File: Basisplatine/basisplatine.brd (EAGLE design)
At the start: 160 x 100 mm, 27 parts, among them IC1 RASPBERRY_PI_ZERO_W__V1.3_, IC2 MEGA8-AI

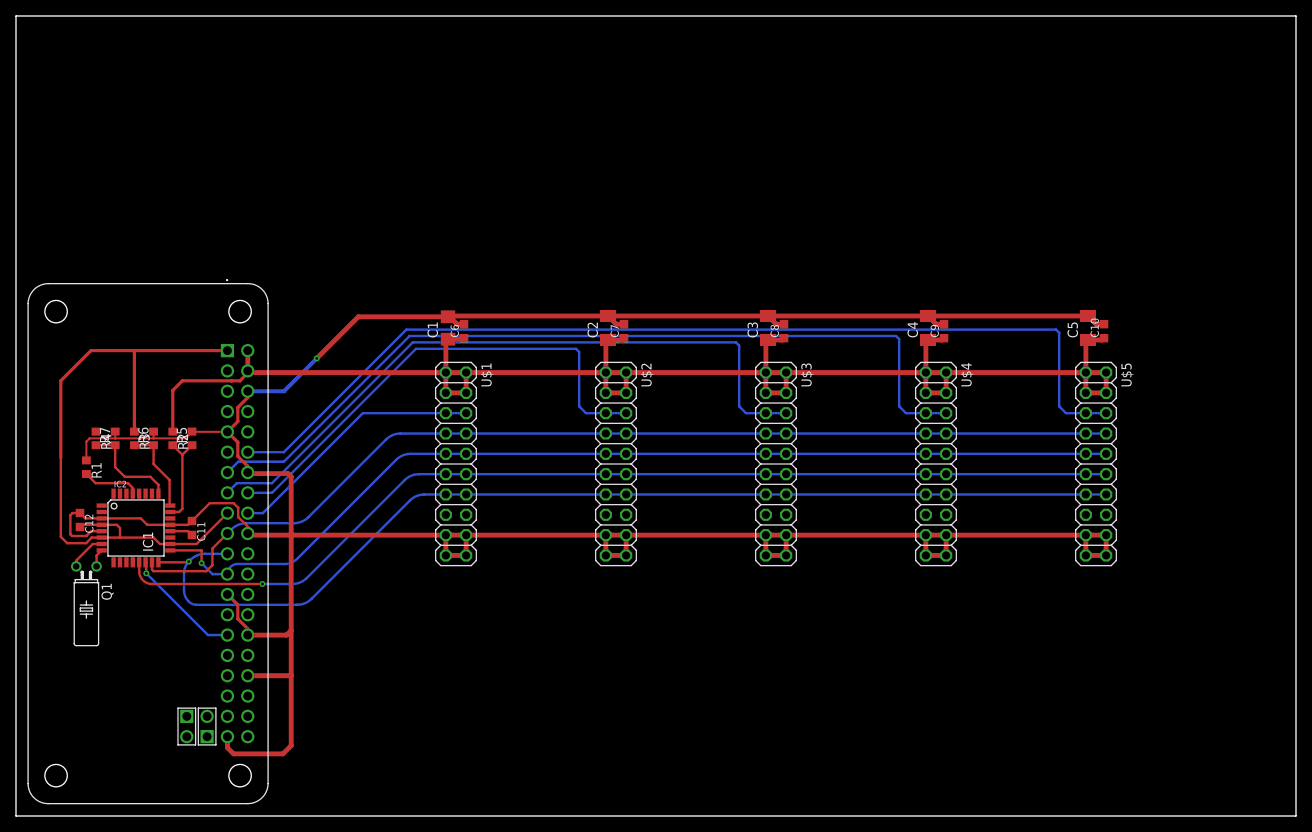
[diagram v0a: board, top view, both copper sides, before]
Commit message: added battery managment
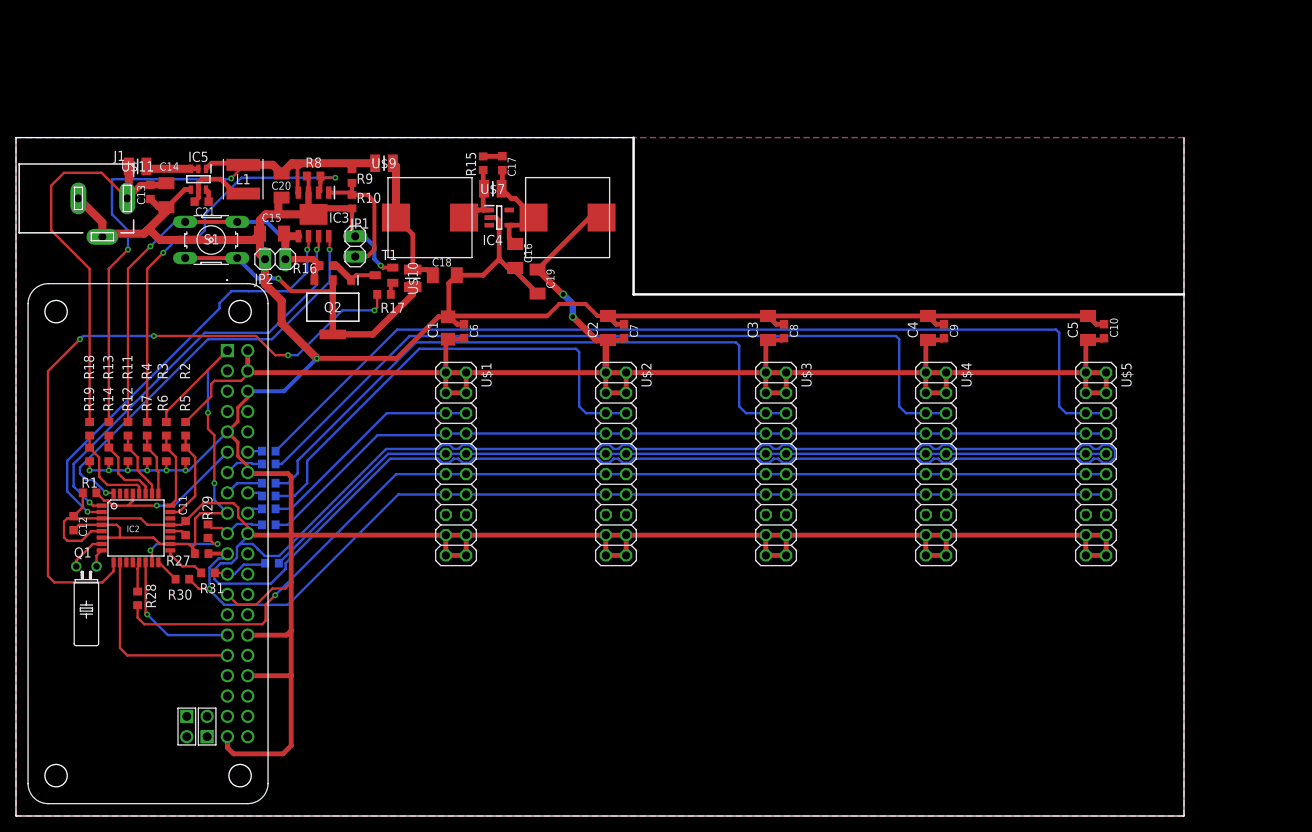
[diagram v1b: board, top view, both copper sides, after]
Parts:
- added C13: 100n, rcl:C0603K
- added C14, C15, C16, C19, C20: 10u, rcl:C1206K
- added C17, C21: 120p, rcl:C0603K
- added C18: 2u2, rcl:C1206K
- added IC3: DIO5158XS8, basisplatine_lib:SOIC127P600X170-9N
- added IC4: TPS613222ADBVR, basisplatine_lib:SOT95P280X145-5N
- added IC5: AP63205WU-7, basisplatine_lib:SOT95P280X100-6N
- added J1: DCJ0202, con-jack:DCJ0202
- added JP1, JP2: (no value), pinhead:1X02
- added L1: SRN5040TA-4R7M, basisplatine_lib:SRN5040TA4R7M
- added Q2: NTF5P03T3G, basisplatine_lib:SOT230P700X175-4N
- added R10, R11, R12, R13, R14, R18, R19, R9: (no value), rcl:R0603
- added R15: 5R, rcl:R0603
- added R16, R17, R29, R30, R31: 10k, rcl:R0603
- added R20, R21, R22, R23, R24, R25, R26, R28: 100R, rcl:R0603
- added R27: 2k, rcl:R0603
- added R8: 1218R, rcl:R0603
- added S1: (no value), switch-omron:B3F-10XX
- added T1: (no value), transistor:SOT23-BEC
- added U$10, U$11, U$7, U$9: SK1035-TP, basisplatine_lib:INDC2520X120N
- added U$6, U$8: SRP1038C-2R2M, basisplatine_lib:SRP1038C-2R2M
- moved R4 6.51 mm to (16.4, 48.4)
- moved R7 4.47 mm to (16.4, 45.2), turned to 270 degrees
- moved R3 4.18 mm to (18.8, 48.4)
- moved R1 3.22 mm to (9.20, 40.4), turned to 0 degrees
- moved R6 2.56 mm to (18.8, 45.2), turned to 270 degrees
- moved R5 2.15 mm to (21.2, 45.2), turned to 270 degrees
- moved R2 2.00 mm to (21.2, 48.4)
- moved C12 0.89 mm to (7.20, 36.6)
- moved C11 0.80 mm to (21.2, 36.0)
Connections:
- net N$7 renamed ADC0
- net N$8 renamed ADC1
- net N$9 renamed ADC2
- new net ADC3: IC2.26, R11.2, R12.1
- new net ADC4: IC2.27, R13.2, R14.1
- new net ADC5: IC2.28, R18.2, R19.1
- new net BOOST_EN: IC2.9, R17.2
- new net CHARGE_EN: IC2.32, IC3.8
- new net ISET: IC3.2, R4.1, R8.2
- new net N$1: IC4.1, R15.2, U$6.P$2, U$7.1
- new net N$10: Q2.1, R16.2, T1.C
- new net N$11: R17.1, T1.B
- new net N$12: Q2.2, Q2.4, S1.1, S1.2, U$10.1
- new net N$13: C21.2, IC5.6
- new net N$15: IC1.18, R22.1
- new net N$16: IC1.16, R23.1
- new net N$17: IC1.15, R24.1
- new net N$18: IC1.13, R25.1
- new net N$19: IC1.12, R26.1
- new net N$20: IC2.13, R28.1
- new net N$21: IC2.15, R29.1
- new net N$22: IC2.16, R30.1
- new net N$23: IC2.17, R31.1
- new net N$5: IC5.2, IC5.3, U$11.2
- new net N$7: C17.1, R15.1
- new net N$8: C16.1, C17.2, IC4.4, U$7.2, U$8.P$1
- new net N$9: C18.1, U$10.2, U$6.P$1, U$9.2
- new net SHUTDOWN: IC1.31, IC2.10
- new net SPI_CLK_R: IC1.23, R20.2, R31.2
- new net SPI_MOSI_R: IC1.19, R21.1, R29.2
- new net STATUS_CHARGE: IC2.1, IC3.7
- new net STATUS_DONE: IC2.2, IC3.6
- new net TEMP: IC3.1, JP1.2, R10.2, R9.1
- new net VIN: C20.1, IC3.4, IC5.1, L1.2, R13.1, R9.2, U$9.1
- new net VJACK: C13.2, C14.1, J1.1, R18.1, U$11.1
- net +3V3: now also R27.2
- net +5V: now also C19.1, U$8.P$2
- net CLOCK_EN: now also IC1.11
- net GND: now also C13.1, C14.2, C15.2, C16.2, C18.2, C19.2, C20.2, IC3.3, IC3.9, IC4.2, IC5.4, J1.2, J1.3, JP1.1, JP2.2, R10.1, R12.2, R14.2, R19.2, R8.1, T1.E
- net N$6: now also C21.1, IC5.5, L1.1; no longer IC1.11
- net SAMPLE: now also R28.2; no longer IC2.13
- net SPI_CLK: now also R20.1; no longer IC1.23, IC2.17
- net SPI_MISO: now also R27.1, R30.2; no longer IC2.16
- net SPI_MOSI: now also R21.2; no longer IC1.19, IC2.15
- net SS1: now also R22.2; no longer IC1.18
- net SS2: now also R23.2; no longer IC1.16
- net SS3: now also R24.2; no longer IC1.15
- net SS4: now also R25.2; no longer IC1.13
- net SS5: now also R26.2; no longer IC1.12
- net VBAT: now also C15.1, IC3.5, JP2.1, Q2.3, R11.1, R16.1, S1.3, S1.4; no longer R4.1
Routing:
- net GND: track 401.2 -> 780.9 mm, vias 1 -> 8
- net VIN: track 0.00 -> 93.0 mm, vias 0 -> 2
- net BOOST_EN: track 0.00 -> 83.9 mm, vias 0 -> 4
- net VBAT: track 0.00 -> 56.4 mm, vias 0 -> 1
- net STATUS_DONE: track 0.00 -> 53.9 mm, vias 0 -> 2
- net STATUS_CHARGE: track 0.00 -> 53.2 mm, vias 0 -> 2
- net ISET: track 0.00 -> 52.8 mm, vias 0 -> 2
- net VJACK: track 0.00 -> 52.8 mm
- net CHARGE_EN: track 0.00 -> 52.6 mm, vias 0 -> 2
- net N$12: track 0.00 -> 39.9 mm, vias 0 -> 1
- net SHUTDOWN: track 0.00 -> 24.5 mm
- net +5V: track 195.8 -> 215.3 mm, vias 0 -> 2
- net SPI_MOSI: track 128.1 -> 108.8 mm
- net +3V3: track 81.9 -> 62.7 mm, vias 0 -> 2
- net N$9: track 0.00 -> 17.1 mm
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- added copper zone on layer 1, net GND
- added copper zone on layer 16, net GND
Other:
- board size 160 x 100 mm -> 146 x 84.8 mm

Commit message: Added dampening Cs on SPI and RJ45
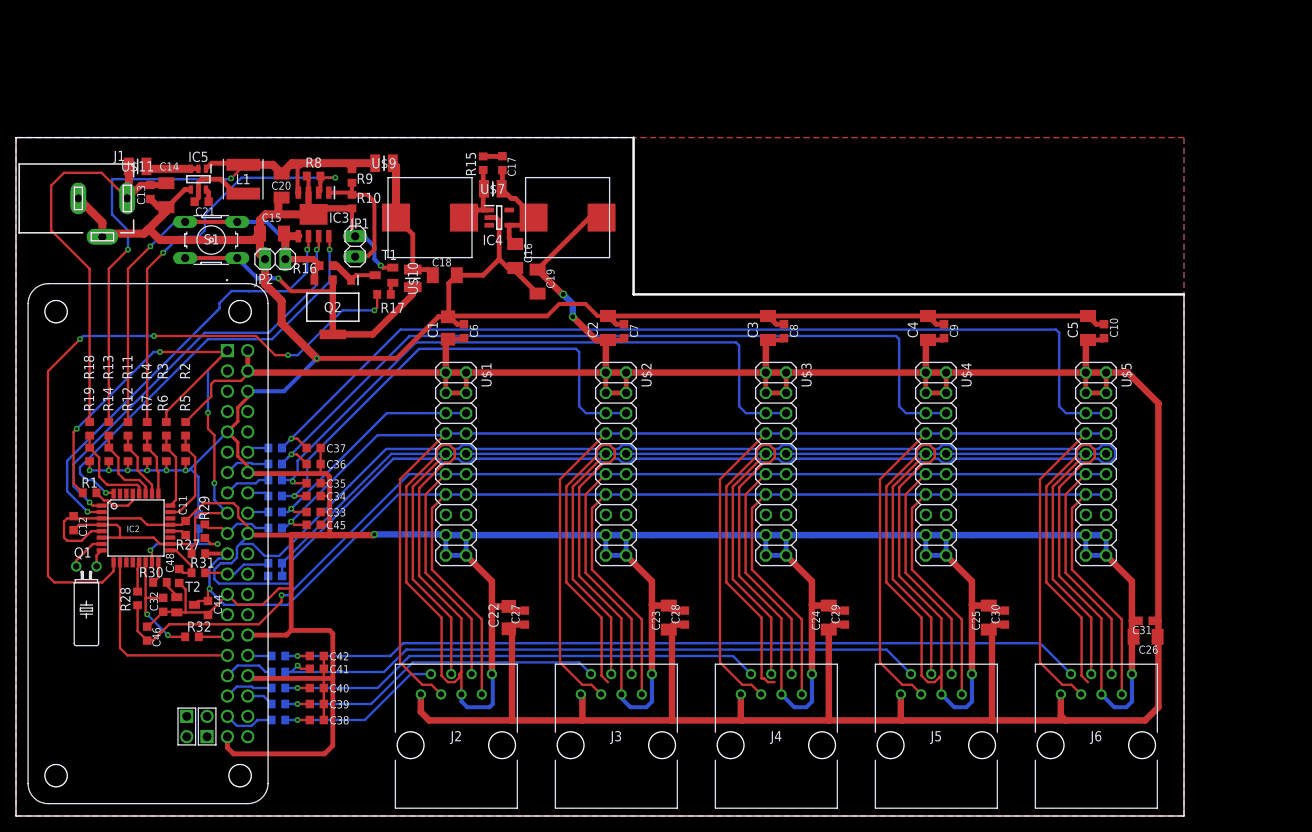
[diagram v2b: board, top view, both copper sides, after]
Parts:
- added C22: (no value), rcl:C1206
- added C23, C24, C25, C26: 2u2, rcl:C1206K
- added C27, C28, C29, C30, C31: 100n, rcl:C0603K
- added C32, C33, C34, C35, C36, C37, C38, C39, C40, C41, C42, C43, C44, C45, C46, C47, C48: (no value), rcl:C0603K
- added J2, J3, J4, J5, J6: 54601-908WPLF, basisplatine_lib:54601908WPLF
- added R32, R33, R34, R35, R36, R37: 100R, rcl:R0603
- added T2: (no value), transistor:SOT23-BEC
- moved R30 2.83 mm to (18.0, 29.2)
- moved R31 1.20 mm to (22.8, 30.4)
- moved R21 0.89 mm to (32.4, 36.0)
- moved R22 0.89 mm to (32.4, 38.0)
- moved R24 0.89 mm to (32.4, 42.0)
- moved R26 0.89 mm to (32.4, 46.0)
- moved R23 0.80 mm to (32.4, 40.0)
- moved R25 0.80 mm to (32.4, 44.0)
- moved R20 0.40 mm to (32.4, 31.6)
- moved R27 0.40 mm to (22.8, 32.8)
- moved R29 0.40 mm to (23.6, 35.6)
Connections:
- removed net N$21: IC2.15, R29.1
- removed net N$23: IC2.17, R31.1
- new net N$14: R30.2, T2.B
- new net N$24: IC1.29, R32.2
- new net N$25: IC1.32, R37.2
- new net N$26: IC1.33, R36.2
- new net N$27: IC1.35, R35.2
- new net N$28: IC1.36, R34.2
- new net N$29: IC1.37, R33.2
- new net SPI_CLK_ATMEGA: C48.2, IC2.17, R31.1
- new net SPI_MOSI_ATMEGA: C47.2, IC2.15, R29.1
- new net SS10: C42.2, J6.2, R37.1
- new net SS6: C38.2, J2.2, R33.1
- new net SS7: C39.2, J3.2, R34.1
- new net SS8: C40.2, J4.2, R35.1
- new net SS9: C41.2, J5.2, R36.1
- net +3V3: now also R1.1
- net +5V: now also C22.1, C23.1, C24.1, C25.1, C26.1, C27.1, C28.1, C29.1, C30.1, C31.1, J2.1, J3.1, J4.1, J5.1, J6.1
- net CLOCK_EN: no longer IC1.11
- net GND: now also C22.2, C23.2, C24.2, C25.2, C26.2, C27.2, C28.2, C29.2, C30.2, C31.2, C32.1, C33.1, C34.1, C35.1, C36.1, C37.1, C38.1, C39.1, C40.1, C41.1, C42.1, C43.1, C44.1, C45.1, C46.1, C47.1, C48.1, J2.5, J2.8, J3.5, J3.8, J4.5, J4.8, J5.5, J5.8, J6.5, J6.8, T2.E; no longer R1.1
- net SAMPLE: now also C46.2, J2.6, J3.6, J4.6, J5.6, J6.6
- net SPI_CLK: now also C43.2, J2.4, J3.4, J4.4, J5.4, J6.4
- net SPI_MISO: now also C44.2, J2.7, J3.7, J4.7, J5.7, J6.7, T2.C; no longer R30.2
- net SPI_MOSI: now also C45.2, J2.3, J3.3, J4.3, J5.3, J6.3
- net SS0: now also C32.2, R32.1; no longer IC1.29
- net SS1: now also C33.2
- net SS2: now also C34.2
- net SS3: now also C35.2
- net SS4: now also C36.2
- net SS5: now also C37.2
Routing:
- net GND: track 780.9 -> 1419.7 mm, vias 8 -> 9
- net +5V: track 215.3 -> 537.2 mm
- net SPI_MOSI: track 108.8 -> 299.2 mm, vias 0 -> 1
- net SPI_CLK: track 109.1 -> 266.5 mm
- net SAMPLE: track 131.9 -> 276.0 mm
- net SPI_MISO: track 129.7 -> 272.0 mm
- net SS10: track 0.00 -> 102.0 mm, vias 0 -> 1
- net SS9: track 0.00 -> 83.5 mm, vias 0 -> 1
- net SS8: track 0.00 -> 62.3 mm, vias 0 -> 1
- net SS7: track 0.00 -> 42.5 mm, vias 0 -> 1
- net +3V3: track 62.7 -> 93.8 mm, vias 2 -> 4
- net SS6: track 0.00 -> 22.1 mm, vias 0 -> 1
- net CLOCK_EN: track 21.5 -> 6.35 mm, vias 1 -> 0
- net SPI_MOSI_ATMEGA: track 0.00 -> 14.1 mm, vias 0 -> 2
- net N$21: track 11.8 -> 0.00 mm, vias 2 -> 0
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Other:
- outline, holes or cut-outs redrawn
